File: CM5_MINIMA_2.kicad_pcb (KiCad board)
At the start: 6 copper layers, 54.6 x 57.1 mm, 99 parts, among them J101 USB_C_Receptacle_USB2.0, J501 690-019-298-412, J502 I2C, J503 SPI, J601 JST_SHBM04B-SRSS-TB, J701 Bus_M.2_Socket_M, J802 Conn_01x22_Female, SW602 B3U-3000P, T401 7498111120AR, U401 TPD4EUSB30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

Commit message: power symbols
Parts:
- removed U603: 74LVC1G07SE-7, Package_TO_SOT_SMD:SOT-353_SC-70-5
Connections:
- net /HDMI/HDMI_5v renamed HDMI_+5V
- net /PCIe-M2/M2_3v3 renamed M2_3V3
- net /USB/VBUS renamed VBUS_USB2.0
- C601 pad 1: +3V3 -> +3V3_PI
- C602 pad 1: +3V3 -> +3V3_PI
- D606 pad 2: +5V -> +3V3_PI
- J502 pad 6: +3V3 -> +3V3_PI
- J503 pad 1: +3V3 -> +3V3_PI
- J802 pad 22: +3V3 -> +3V3_PI
- Module301 pad 84: +3V3 -> +3V3_PI
- Module301 pad 86: +3V3 -> +3V3_PI
- Module302 pad 109: /CM5/PCIE_nRST -> /CM5/PCIE_PI.nRST
- R102 pad 1: +3V3 -> +3V3_PI
- R501 pad 1: +3V3 -> +3V3_PI
- R502 pad 1: +3V3 -> +3V3_PI
- R606 pad 2: Net-(R606-Pad2) -> /CM5/nLED_ACTIVITY
- R704 pad 1: /PCIe-M2/PCIE_C._PWR_EN -> /CM5/PCIE_PI.PWR_EN
- T401 pad 14: +3V3 -> +3V3_PI
- T401 pad 2: +3V3 -> +3V3_PI
- TP103 pad 1: +3V3 -> +3V3_PI
- U601 pad 1: +3V3 -> +3V3_PI
- U702 pad 7: /PCIe-M2/PCIE_C._PWR_EN -> /CM5/PCIE_PI.PWR_EN
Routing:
- net +3V3_PI: track 0.00 -> 167.7 mm, vias 0 -> 12
- net +3V3: track 157.4 -> 0.00 mm, vias 11 -> 0
- net /CM5/PCIE_PI.nRST: track 0.00 -> 35.6 mm, vias 0 -> 1
- net Net-(R606-Pad2): track 4.89 -> 0.00 mm
- net /CM5/PCIE_PI.nCLKREQ: track 35.8 -> 39.6 mm
- net /CM5/VBUS_EN: track 43.1 -> 46.4 mm
- net /CM5/PCIE_PI.nWAKE: track 36.5 -> 38.9 mm
- net /CM5/nLED_ACTIVITY: track 8.99 -> 7.10 mm
- net /CM5/PCIE_PI.CLK_N: track 54.4 -> 55.7 mm
- net +5V: track 35.2 -> 34.1 mm, vias 26 -> 24
- net /PCIe-M2/PCIE_C._PWR_EN: track 1.02 -> 0.00 mm
- net /CM5/PCIE_PI.PWR_EN: track 0.00 -> 1.02 mm
- net /CM5/PCIE_PI.CLK_P: track 54.3 -> 55.0 mm
- net GND: vias 188 -> 183
- added copper zone on B.Cu, net +3V3_PI
- added copper zone on F.Cu, net +3V3_PI
- removed copper zone on B.Cu, net +3V3
- removed copper zone on F.Cu, net +3V3

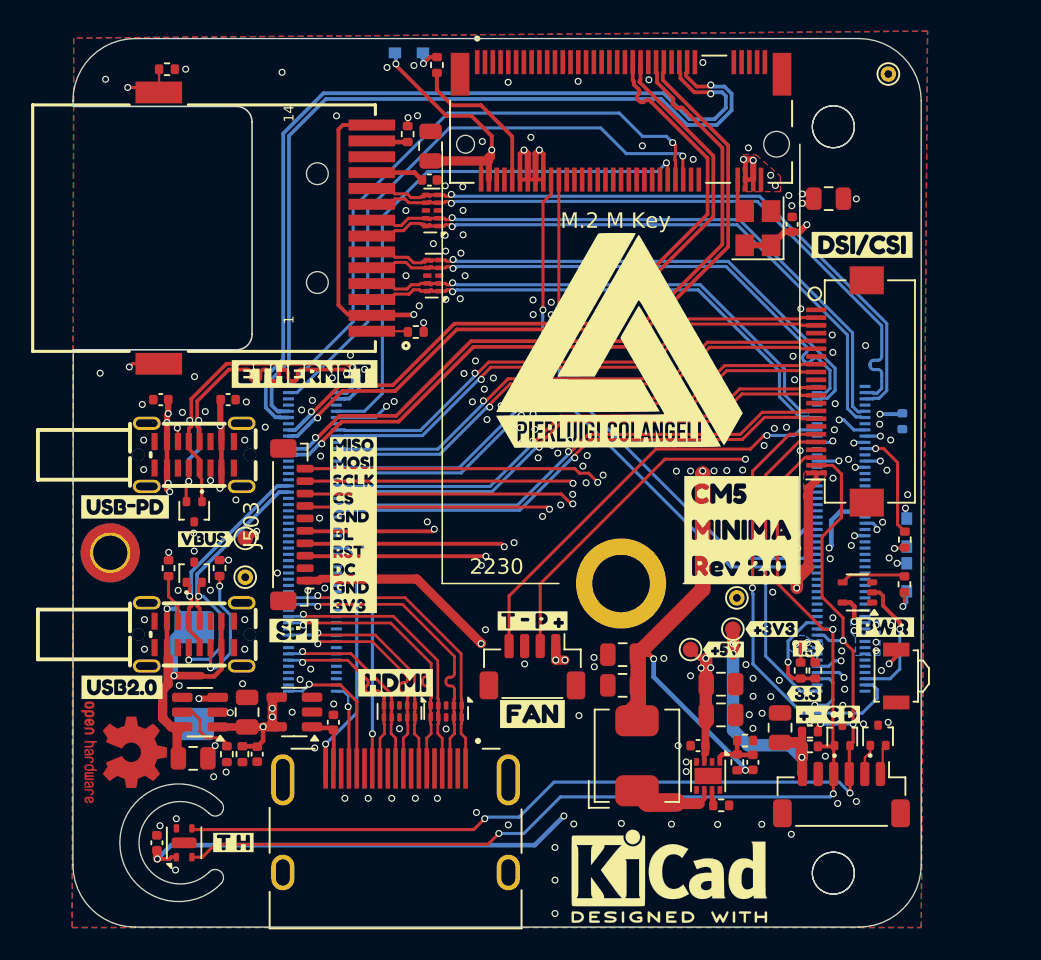
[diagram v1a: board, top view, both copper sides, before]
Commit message: pcie signal corrected
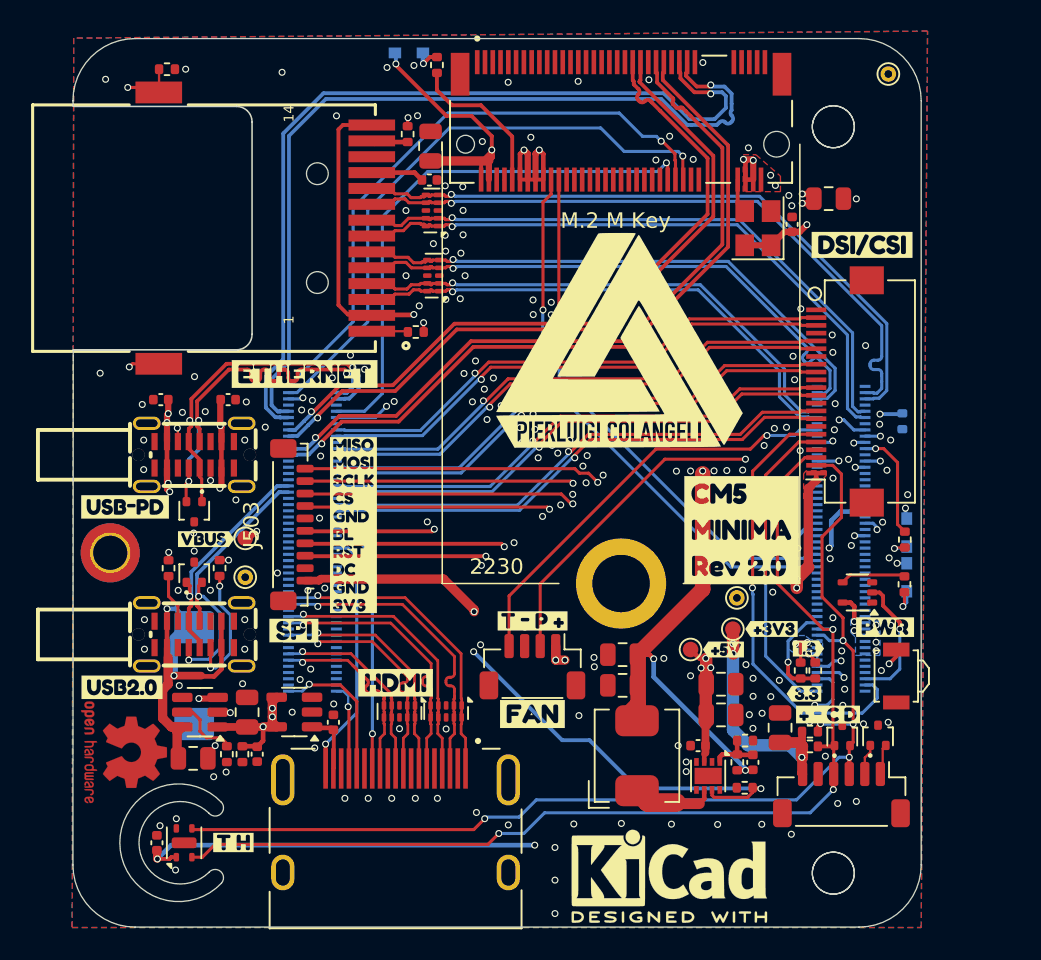
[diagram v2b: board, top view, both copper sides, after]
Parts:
- moved R704 1.89 mm to (121.5, 72.1), turned to 180 degrees
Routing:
- net /CM5/PCIE_PI.PWR_EN: track 1.02 -> 49.5 mm, vias 0 -> 3
- net +3V3_PI: track 167.7 -> 166.8 mm
- net /CM5/PCIE_PI.CLK_P: track 55.0 -> 55.6 mm
- net /CM5/VBUS_EN: track 46.4 -> 47.0 mm
- net GND: vias 183 -> 184

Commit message: save
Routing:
- net +3V3_PI: track 166.8 -> 158.5 mm
- net GND: vias 184 -> 188

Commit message: drc ok
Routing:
- net +3V3_PI: track 158.5 -> 149.4 mm, vias 12 -> 11
- net /CM5/PCIE_PI.PWR_EN: track 49.0 -> 50.5 mm

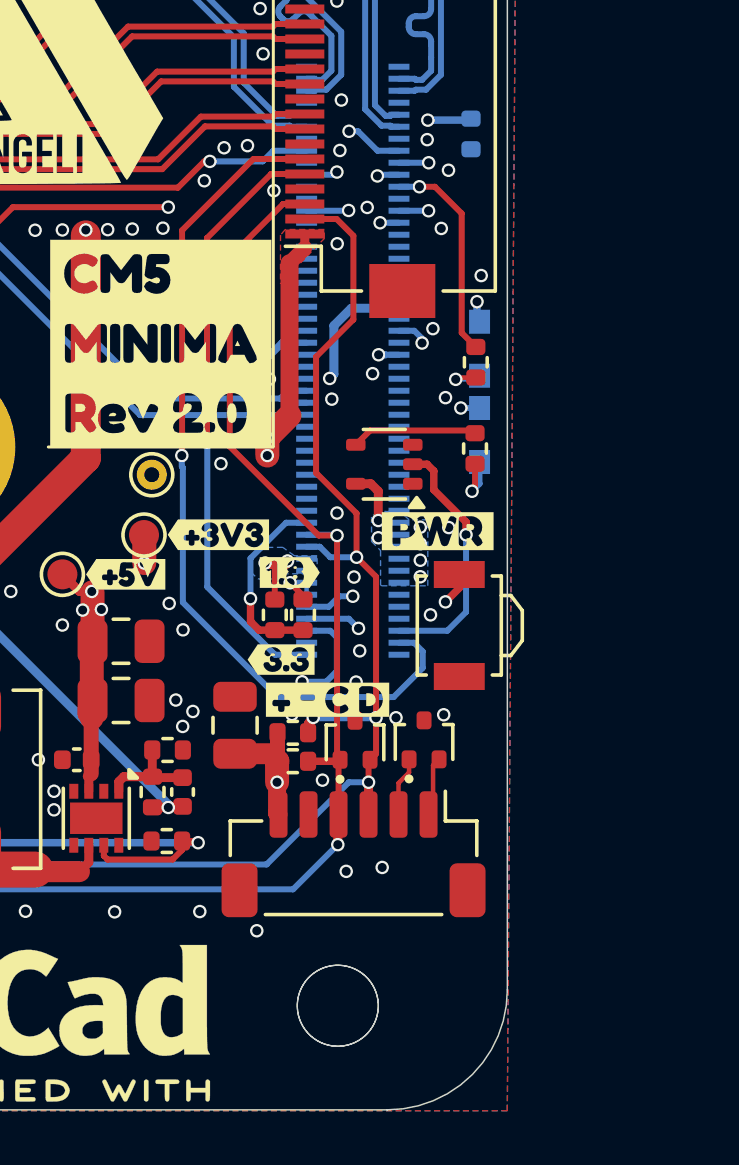
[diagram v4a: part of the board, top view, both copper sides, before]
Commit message: changed i2c connector and nrpiboot
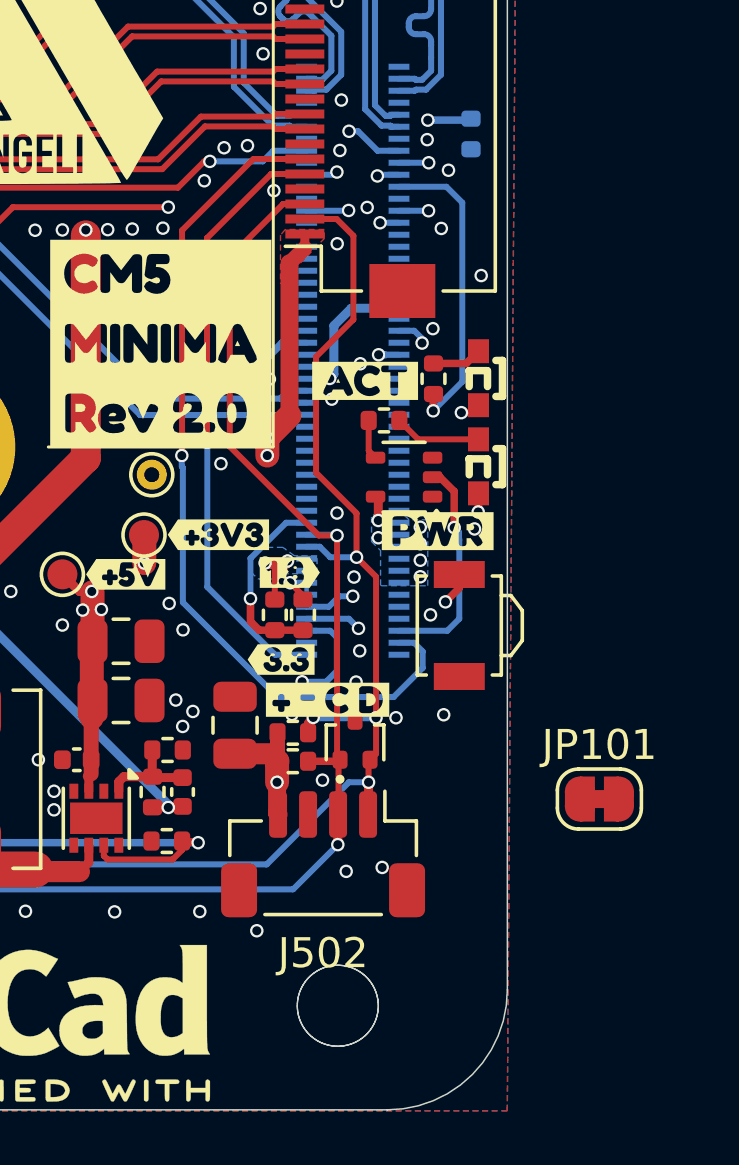
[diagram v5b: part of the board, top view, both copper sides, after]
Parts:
- removed D501: RCLAMP0502BA, Package_TO_SOT_SMD:SOT-416
- removed the kibuzzard-6773B9F7 at (131.7, 61.9)
- added JP101: nRPIBOOT, Jumper:SolderJumper-2_P1.3mm_Bridged_RoundedPad1.0x1.5mm, F.Cu at (136.0, 70.7)
- D605, D606, kibuzzard-6773BA89: moved to F.Cu
- J502: footprint Connector_JST:JST_SH_BM06B-SRSS-TB_1x06-1MP_P1.00mm_Vertical -> Connector_JST:JST_SH_BM04B-SRSS-TB_1x04-1MP_P1.00mm_Vertical
- moved kibuzzard-6773BA89 6.03 mm to (128.2, 56.8), turned to 0 degrees
- moved R605 3.18 mm to (128.8, 58.1), turned to 180 degrees
- moved R606 1.51 mm to (130.4, 56.7), turned to -90 degrees
- moved D605 1.05 mm to (131.9, 59.6), turned to -90 degrees
- moved J502 1.02 mm to (126.8, 72.5)
- moved D606 0.98 mm to (131.9, 56.7), turned to -90 degrees
- moved U602 0.79 mm to (129.5, 60.0)
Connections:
- J502 pad 1: /IO/IO6 -> /SDA
- J502 pad 2: /IO/IO5 -> /SCL
- J502 pad 3: /SDA -> GND
- J502 pad 4: /SCL -> +3V3_PI
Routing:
- net /CM5/nLED_ACTIVITY: track 7.10 -> 10.2 mm
- net Net-(R605-Pad2): track 4.21 -> 1.34 mm
- net +3V3_PI: track 149.4 -> 146.9 mm
- net /IO/IO6: track 1.98 -> 0.00 mm
- net /IO/IO5: track 1.98 -> 0.00 mm
- net /CM5/PI_nLED_PWR: track 8.43 -> 7.41 mm
- net +5V: track 34.1 -> 33.1 mm
- net Net-(D605-K): track 2.03 -> 2.90 mm, vias 1 -> 0
- net Net-(D606-K): track 1.54 -> 1.67 mm, vias 1 -> 0
- net GND: vias 188 -> 187
